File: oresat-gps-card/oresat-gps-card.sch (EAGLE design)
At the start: 371 parts, among them J1 ORESAT-DEBUG-CONNECTOR-CARD, J100 DM3BT-DSF-PEJS, J102 FTSH-105-XX-X-DV-K, J4 TFM-120-01-L-D-RA, Q1 MMBT2907, Q2 PMV45EN, Q3 DMP2240UDM, Q4 PMV45EN, Q5 MOSFET-PCH-SOT23-6, Q6 MOSFET-PCH-SOT23-6, U1 RCLAMP0504FB, U10 TLVH431, U11 TCAN330, U12 MIC842LYC5, U13 MIC842LYC5, U14 MAX4211FETE, U15 TPS62112, U16 MAX7310ATE, U17 25AAXX, U18 RCLAMP0504FB, U19 BP2G+, U2 TPS2051CDBVR, U20 MAX8510EXK29+T, U22 LT1719S6, U23 MAX2771ETI+, U3 THGBMJG7C2LBAU8, U4 SN74LVC1G07DCK, U5 SKY65723-81, U6 7Q-16.368MBG-T, U7 OSD3358-512M-BSM, U8 MAX8510EXK29+T, U9 MAX8510EXK29+T, Y1 24MHz, Y2 ABS07-32.768KHZ-T

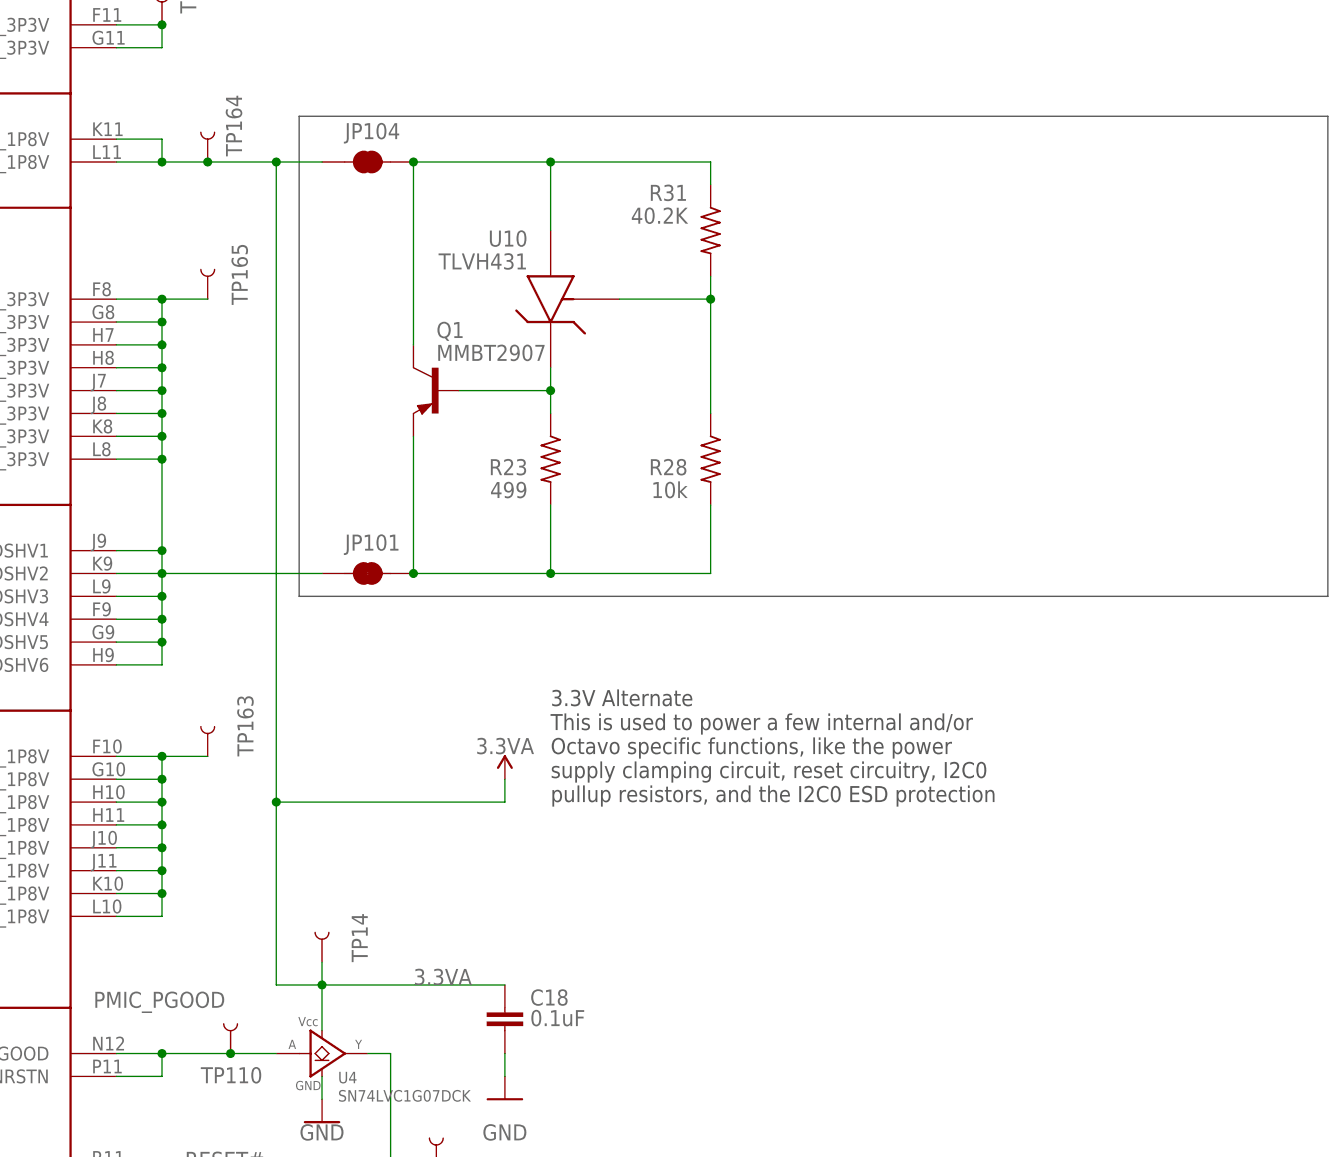
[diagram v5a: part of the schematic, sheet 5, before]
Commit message: Fixed 3.3VA rail for I2C protection chip.
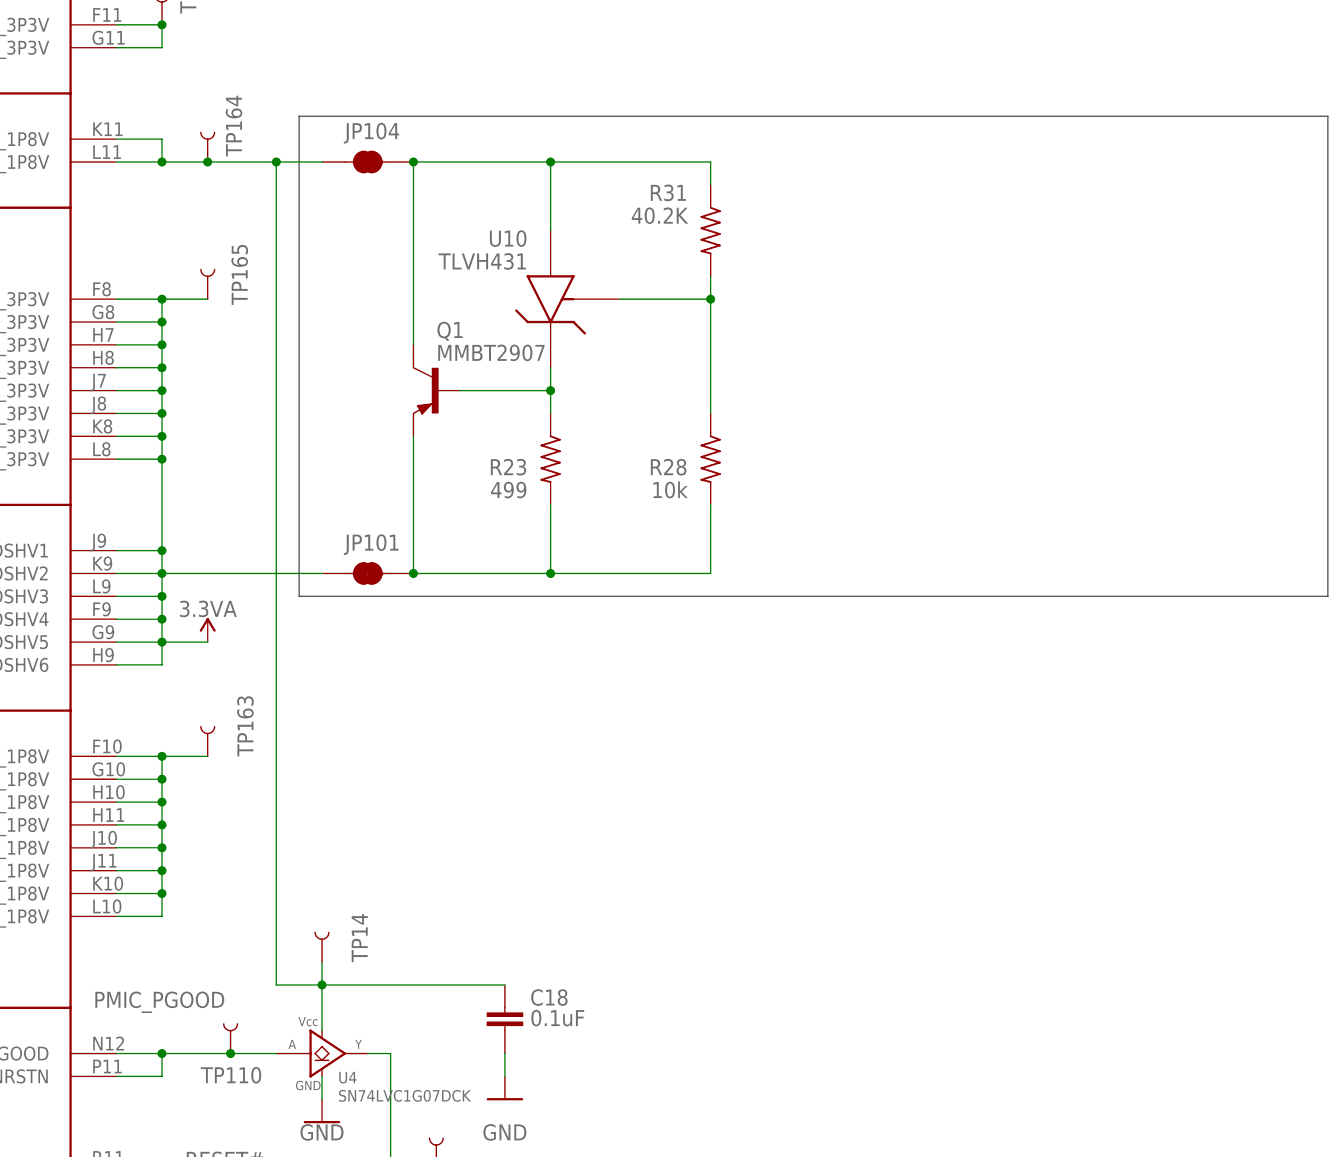
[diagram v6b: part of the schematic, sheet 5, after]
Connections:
- removed net N$26: JP101.1, TP165.1, U7A.SYS_VDD3_3P3V@1, U7A.SYS_VDD3_3P3V@2, U7A.SYS_VDD3_3P3V@3, U7A.SYS_VDD3_3P3V@4, U7A.SYS_VDD3_3P3V@5, U7A.SYS_VDD3_3P3V@6, U7A.SYS_VDD3_3P3V@7, U7A.SYS_VDD3_3P3V@8, U7A.VDDSHV1, U7A.VDDSHV2, U7A.VDDSHV3, U7A.VDDSHV4, U7A.VDDSHV5, U7A.VDDSHV6
- new net N$133: C18.1, JP104.1, TP14.1, TP164.1, U4.VCC, U7A.SYS_RTC_1P8V@1, U7A.SYS_RTC_1P8V@2
- net 3.3VA: now also JP101.1, TP165.1, U7A.SYS_VDD3_3P3V@1, U7A.SYS_VDD3_3P3V@2, U7A.SYS_VDD3_3P3V@3, U7A.SYS_VDD3_3P3V@4, U7A.SYS_VDD3_3P3V@5, U7A.SYS_VDD3_3P3V@6, U7A.SYS_VDD3_3P3V@7, U7A.SYS_VDD3_3P3V@8, U7A.VDDSHV1, U7A.VDDSHV2, U7A.VDDSHV3, U7A.VDDSHV4, U7A.VDDSHV5, U7A.VDDSHV6; no longer C18.1, JP104.1, TP14.1, TP164.1, U4.VCC, U7A.SYS_RTC_1P8V@1, U7A.SYS_RTC_1P8V@2
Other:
- note removed: "3.3V Alternate This is used to power a few internal and/or Octavo specific functions, like the power supply clamping circuit, reset circuitry, I2C0 pullup resistors, and the I2C0 ESD protection"

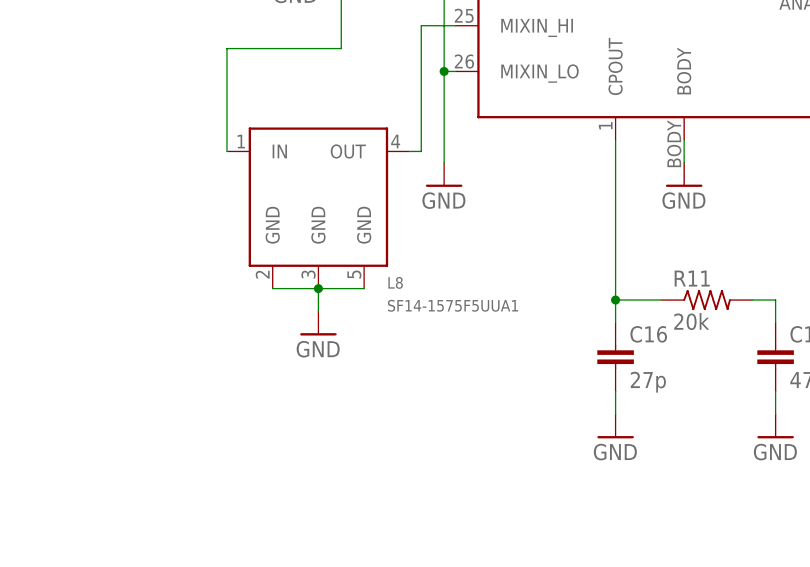
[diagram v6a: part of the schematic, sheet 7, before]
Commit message: Added attributes to some parts, and changed internal cutout polygons to 0.1 width instead of 0 width.
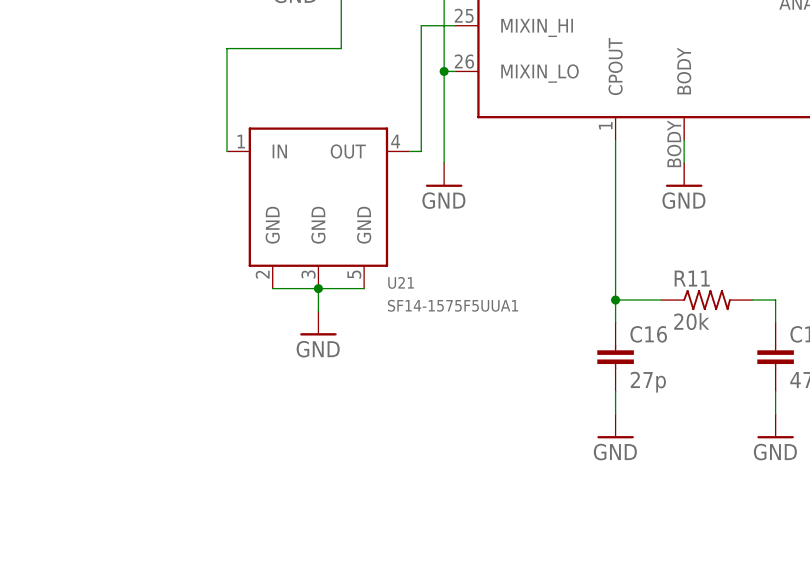
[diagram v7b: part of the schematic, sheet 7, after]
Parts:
- J100: DIS (none) -> Digi-Key; DPN (none) -> HR1942CT-ND; MFR (none) -> Hirose Electric
- SH1: DIS (none) -> Digi-Key; DPN (none) -> 903-1014-ND; MFR (none) -> Laird Technologies EMI; MPN (none) -> BMI-S-202-C
- U20, U8, U9: DIS (none) -> Digi-Key; DPN (none) -> MAX8510EXK29+TCT-ND; MFR (none) -> Maxim Integrated; MPN (none) -> MAX8510EXK29+T
- U21: DIS (none) -> Digi-Key; DPN (none) -> 478-6834-1-ND; MFR (none) -> Kyocera International; MPN (none) -> SF14-1575F5UUA1
- U23: DIS (none) -> Digi-Key; DPN (none) -> MAX2771ETI+-ND; MFR (none) -> Maxim Integrated; MPN (none) -> MAX2771ETI+
- U5: DIS (none) -> Digi-Key; DPN (none) -> 863-2063-1-ND; MFR (none) -> Skyworks Solutions; MPN (none) -> SKY65723-81
- U6: MFR (none) -> TXC Corporation
- renumbered L8 to U21, LED7 to D10, U$8 to U24

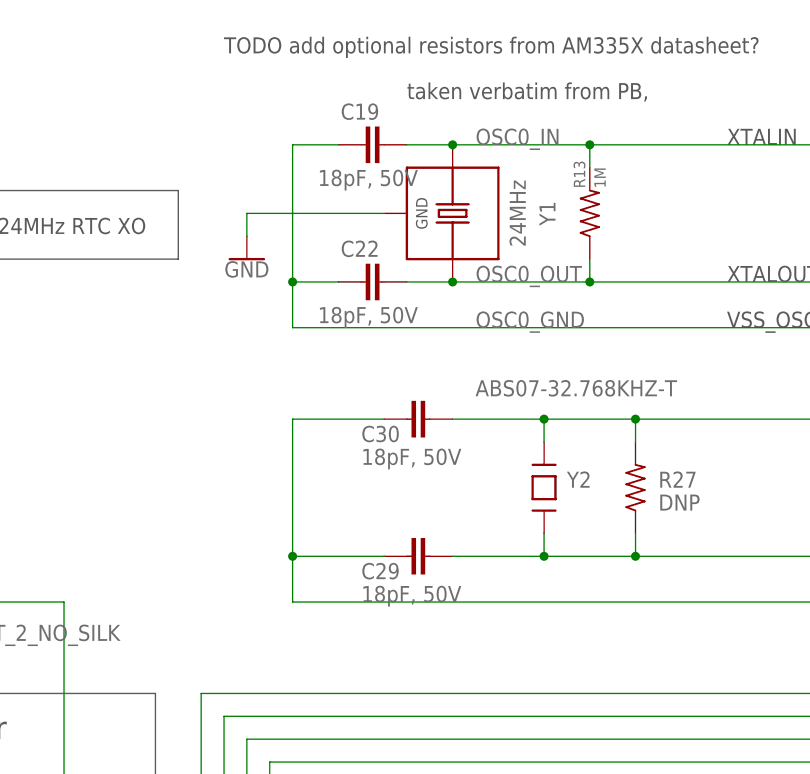
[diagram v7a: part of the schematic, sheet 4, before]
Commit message: Updated oscillator capacitor values and added BOM
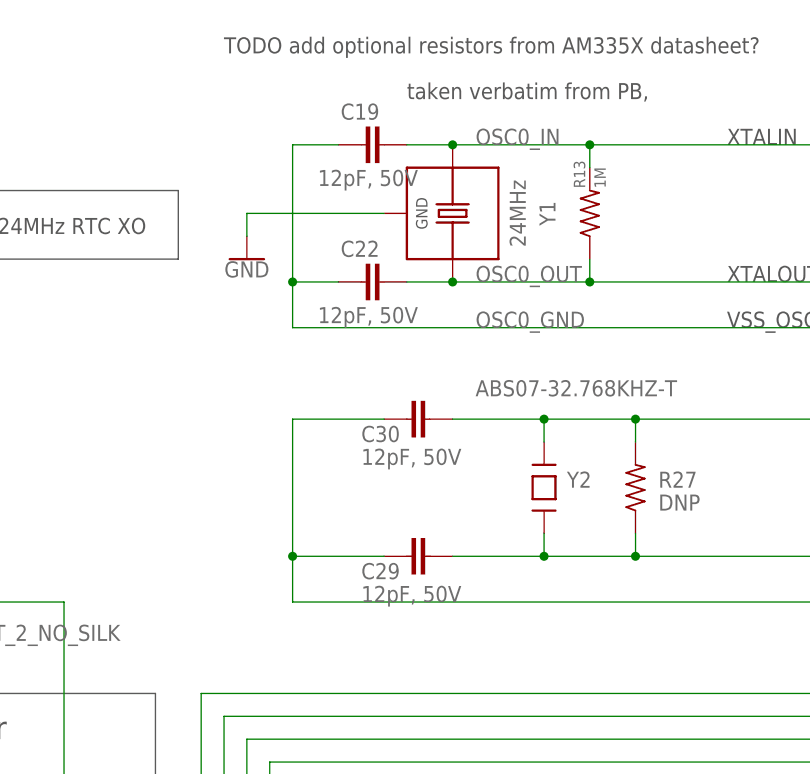
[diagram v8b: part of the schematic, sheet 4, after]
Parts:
- C19, C22, C29, C30: value 18pF, 50V -> 12pF, 50V
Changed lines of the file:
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@@
 <part name="GND70" library="SparkFun-PowerSymbols" deviceset="GND" device=""/>
 <part name="GND72" library="SparkFun-PowerSymbols" deviceset="GND" device=""/>
-<part name="C22" library="oresat-rcl" deviceset="C-EU" device="0603-A" value="18pF, 50V"/>
-<part name="C19" library="oresat-rcl" deviceset="C-EU" device="0603-A" value="18pF, 50V"/>
+<part name="C22" library="oresat-rcl" deviceset="C-EU" device="0603-A" value="12pF, 50V"/>
+<part name="C19" library="oresat-rcl" deviceset="C-EU" device="0603-A" value="12pF, 50V"/>
 <part name="R13" library="oresat-rcl" deviceset="R-US_" device="0603-A" value="1M"/>
 <part name="J102" library="J-Samtec-FTSH-105-XXX-DV-K-ARM-SWD" deviceset="FTSH-105-XX-X-DV-K" device=""/>
@@
 <part name="GND75" library="SparkFun-PowerSymbols" deviceset="GND" device=""/>
 <part name="R27" library="oresat-rcl" deviceset="R-US_" device="0603-A" value="DNP"/>
-<part name="C30" library="oresat-rcl" deviceset="C-EU" device="0603-A" value="18pF, 50V"/>
-<part name="C29" library="oresat-rcl" deviceset="C-EU" device="0603-A" value="18pF, 50V"/>
+<part name="C30" library="oresat-rcl" deviceset="C-EU" device="0603-A" value="12pF, 50V"/>
+<part name="C29" library="oresat-rcl" deviceset="C-EU" device="0603-A" value="12pF, 50V"/>
 <part name="Y2" library="OSD3358-SM-RED Platform" deviceset="ABS07-32.768KHZ-T" device=""/>
 <part name="TP168" library="SparkFun-Connectors" deviceset="TEST-POINT" device="3X4" package3d_urn="urn:adsk.eagle:package:38287/1"/>
